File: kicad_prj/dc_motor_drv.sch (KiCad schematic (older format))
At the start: 20 parts

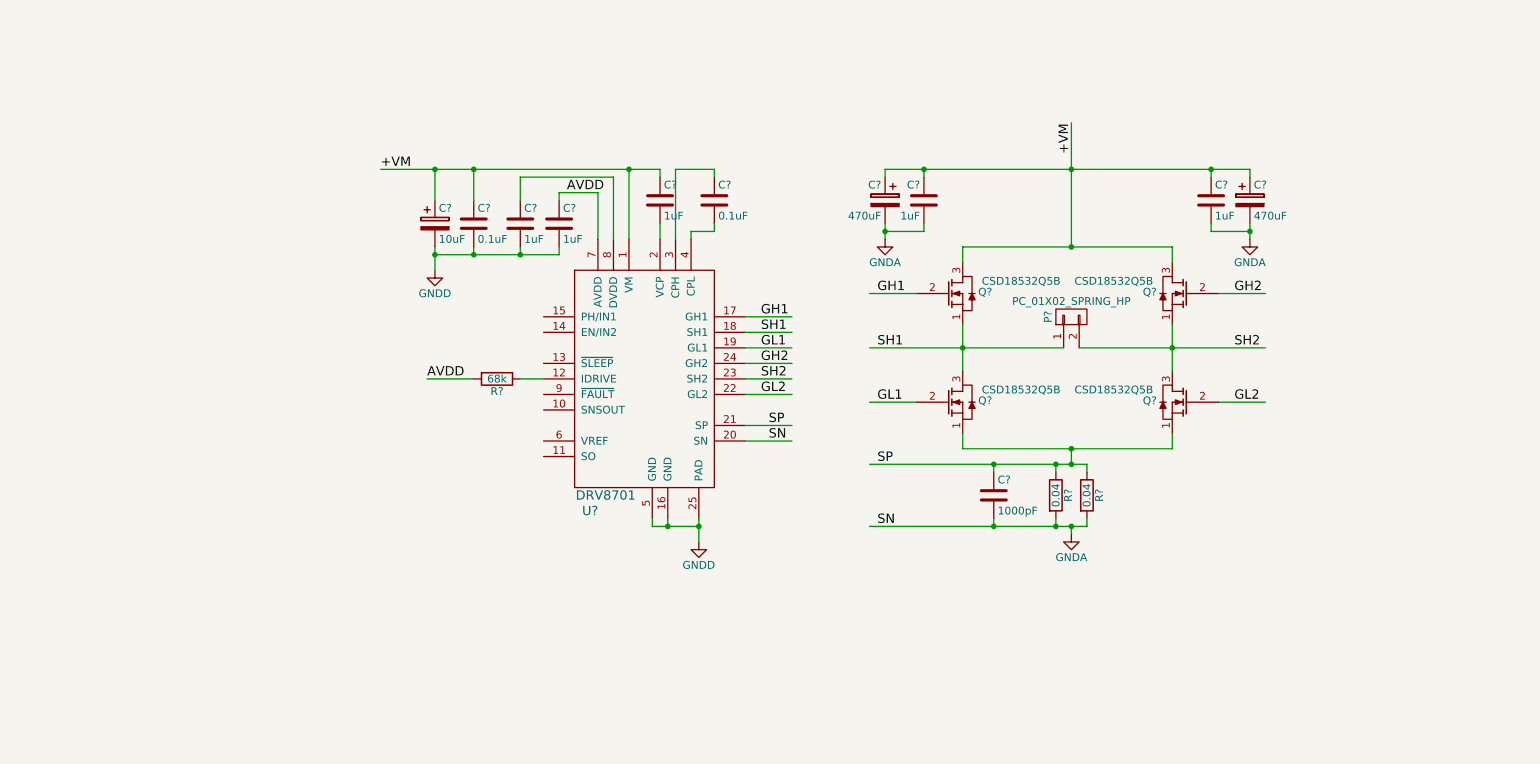
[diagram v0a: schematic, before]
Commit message: Schematics 3
Added spindle driver and sensors/limit switches.
Need to add terminals for ADC channels.
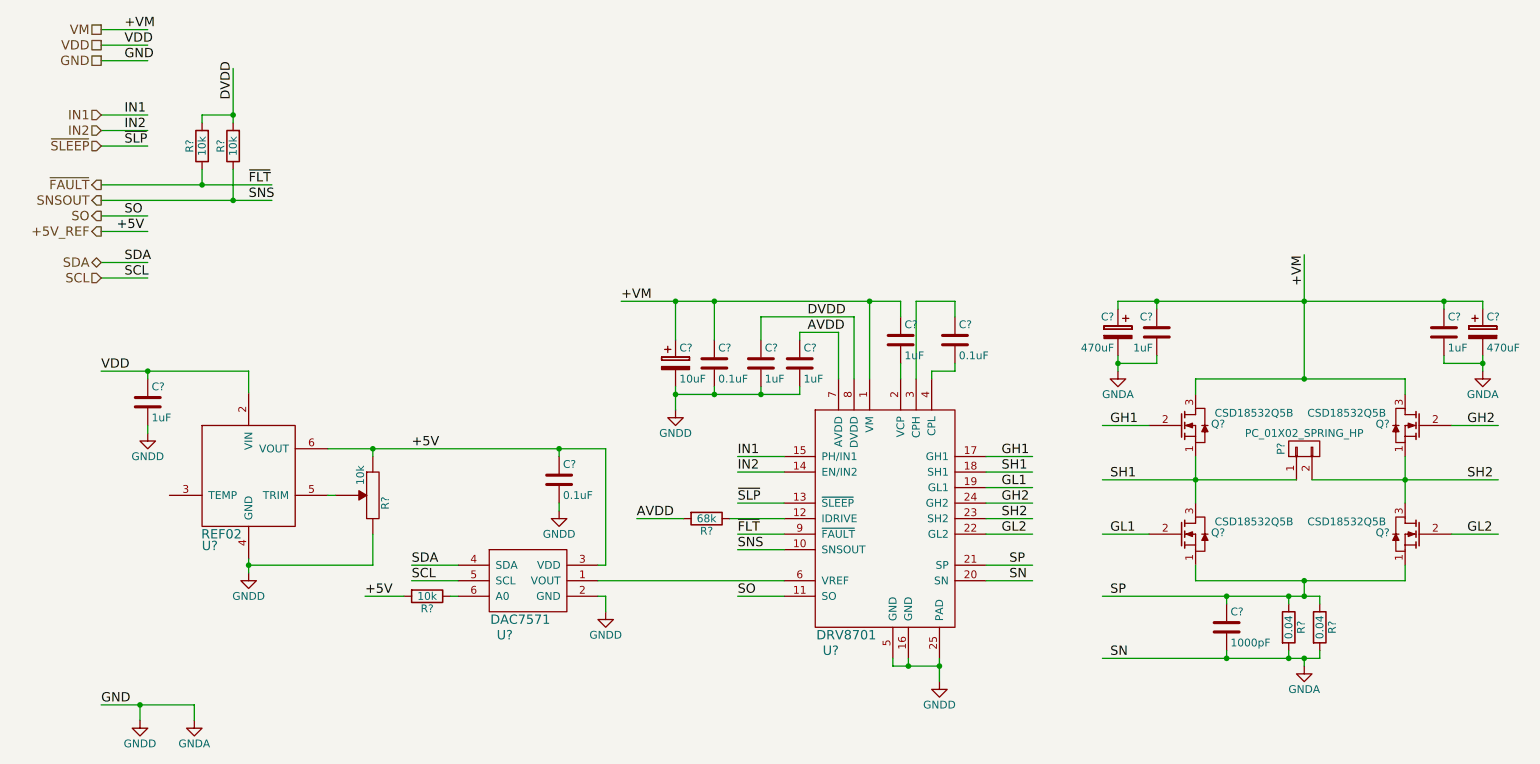
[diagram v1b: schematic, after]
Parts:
- added C?: 1uF, symbol C
- added C?: 0.1uF, symbol C
- added R?: 10k, symbol RTRM
- added R? (x3): 10k, symbol R
- added U?: DAC7571, symbol DAC7571
- added U?: REF02, symbol REF02
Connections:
- net labels added: +5V, +5V_REF, DVDD, GND, IN1, IN2, SCL, SDA, SNS, SNSOUT, SO, VDD, VM, ~FAULT, ~FLT, ~SLEEP, ~SLP
- wire segments 99 -> 120
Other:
- moved on the sheet: C?, P?, Q?, R?, U?

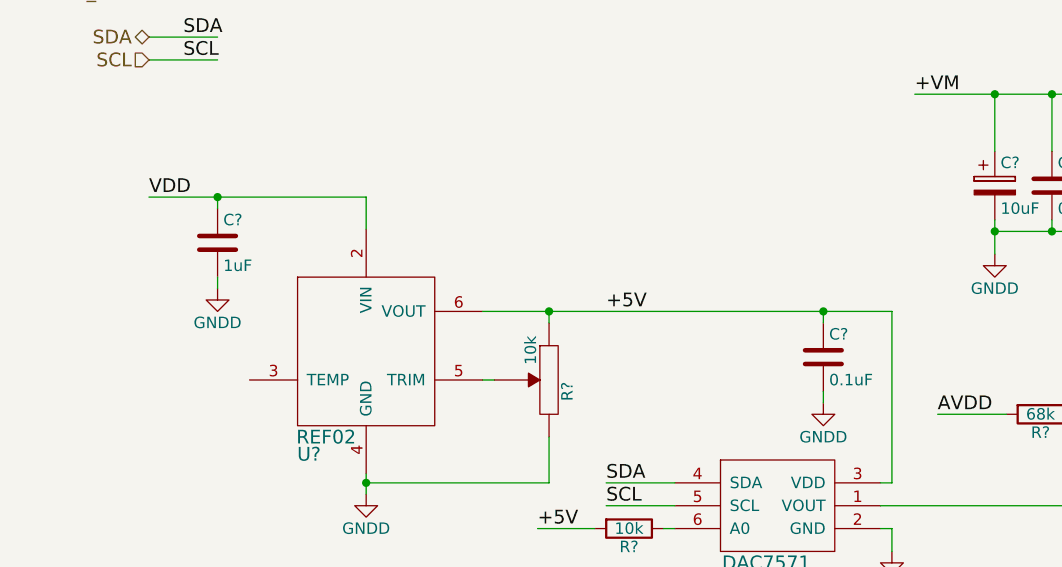
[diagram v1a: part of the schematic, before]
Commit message: Schematics 4
Finished sensor inputs.
Added DAC for stepper motor drivers.
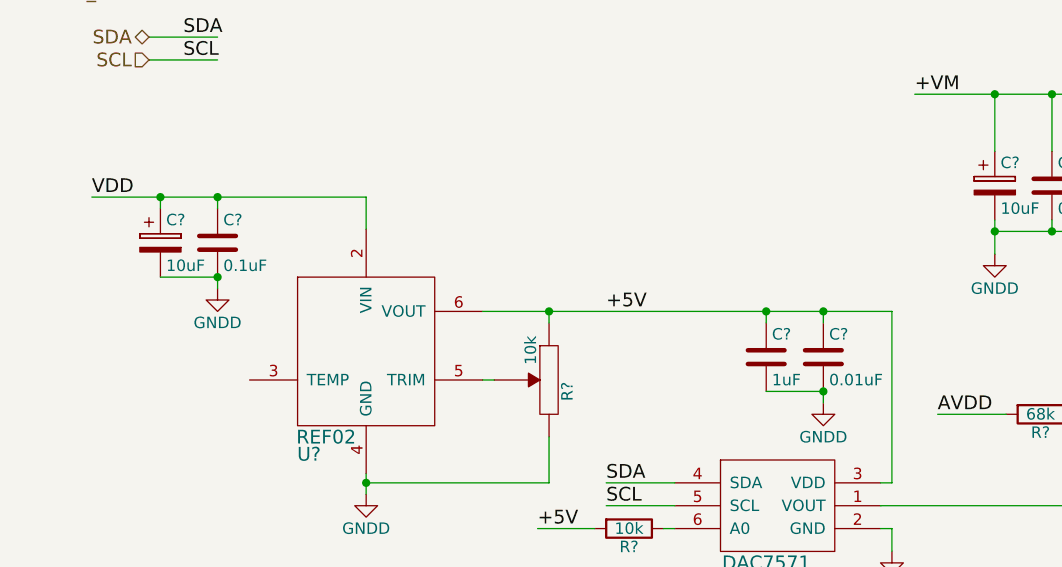
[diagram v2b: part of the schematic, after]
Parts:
- added C?: 1uF, symbol C
- added C?: 10uF, symbol CP
- C?: value 1uF -> 0.1uF
- C?: value 0.1uF -> 0.01uF
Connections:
- wire segments 120 -> 124
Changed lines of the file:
@@
 $Descr A4 11693 8268
 encoding utf-8
-Sheet 6 7
+Sheet 6 8
 Title ""
 Date ""
@@
 P 1750 3800
 F 0 "C?" H 1775 3900 50  0000 L CNN
-F 1 "1uF" H 1775 3700 50  0000 L CNN
+F 1 "0.1uF" H 1775 3700 50  0000 L CNN
 F 2 "" H 1788 3650 30  0000 C CNN
 F 3 "" H 1750 3800 60  0000 C CNN
@@
 	2400 3600 2400 3740
 Wire Wire Line
-	1450 3600 2400 3600
+	1200 3600 2400 3600
 Wire Wire Line
 	1750 3650 1750 3600
 Connection ~ 1750 3600
-Text Label 1450 3600 0    60   ~ 0
+Text Label 1200 3600 0    60   ~ 0
 VDD
 $Comp
@@
 P 4400 4300
 F 0 "C?" H 4425 4400 50  0000 L CNN
-F 1 "0.1uF" H 4425 4200 50  0000 L CNN
+F 1 "0.01uF" H 4425 4200 50  0000 L CNN
 F 2 "" H 4438 4150 30  0000 C CNN
 F 3 "" H 4400 4300 60  0000 C CNN
@@
 Wire Wire Line
 	4400 4500 4400 4450
+$Comp
+L C C?
+U 1 1 565613C4
+P 4150 4300
+F 0 "C?" H 4175 4400 50  0000 L CNN
+F 1 "1uF" H 4175 4200 50  0000 L CNN
+F 2 "" H 4188 4150 30  0000 C CNN
+F 3 "" H 4150 4300 60  0000 C CNN
+	1    4150 4300
+	1    0    0    -1
+$EndComp
+Wire Wire Line
+	4150 4150 4150 4100
+Connection ~ 4150 4100
+Wire Wire Line
+	4400 4450 4150 4450
+Connection ~ 4400 4450
+$Comp
+L CP C?
+U 1 1 565FCB4C
+P 1500 3800
+F 0 "C?" H 1525 3900 50  0000 L CNN
+F 1 "10uF" H 1525 3700 50  0000 L CNN
+F 2 "" H 1538 3650 30  0000 C CNN
+F 3 "" H 1500 3800 60  0000 C CNN
+	1    1500 3800
+	1    0    0    -1
+$EndComp
+Wire Wire Line
+	1500 3650 1500 3600
+Connection ~ 1500 3600
+Wire Wire Line
+	1500 3950 1750 3950
+Connection ~ 1750 3950
 $EndSCHEMATC

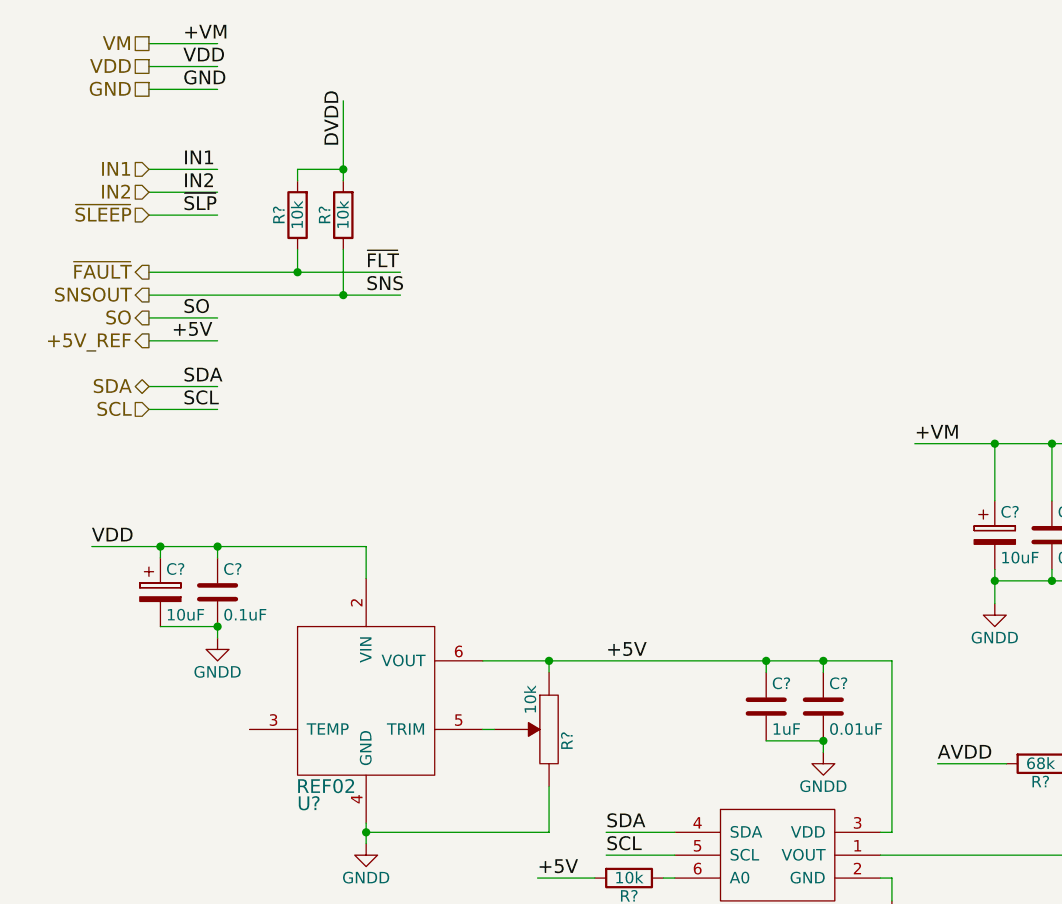
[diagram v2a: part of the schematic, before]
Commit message: Schematics 5
Started isolation part.
Selected ICs for SPI isolation and general digital I/Os.
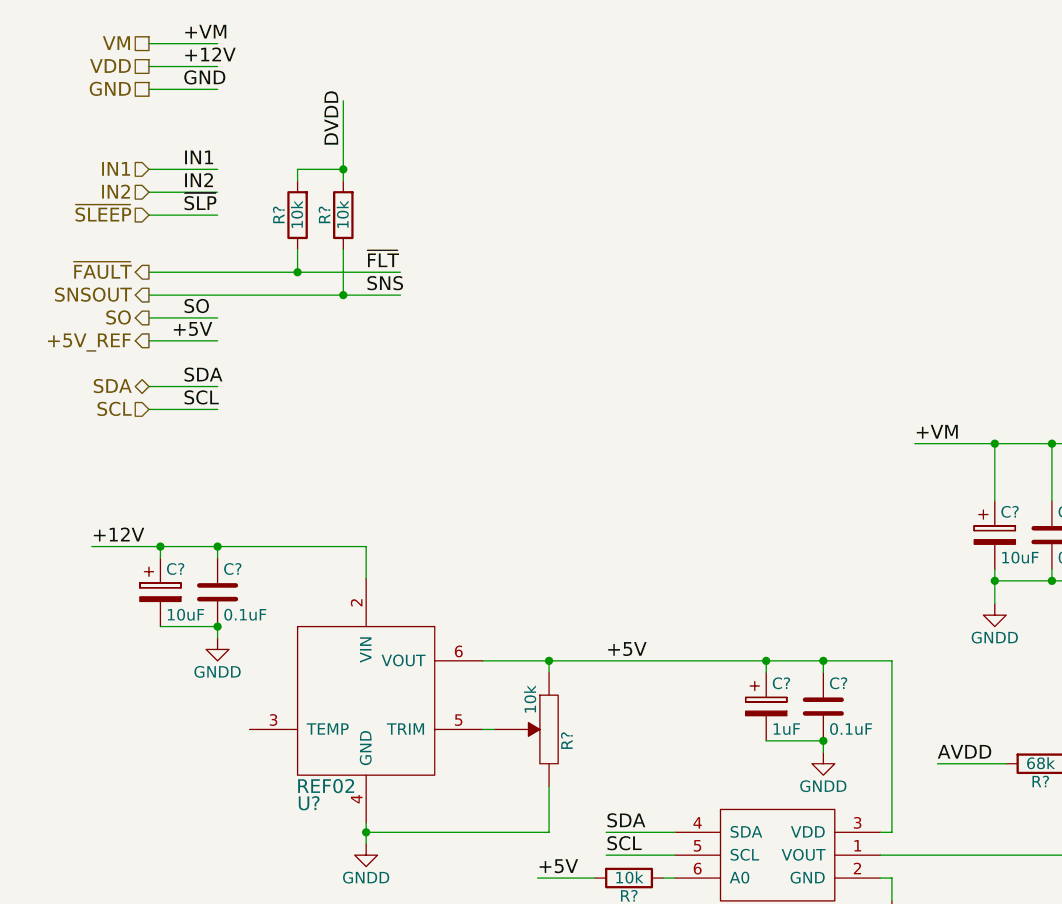
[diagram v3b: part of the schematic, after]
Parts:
- removed C?: 1uF, symbol C
- removed C?: 0.01uF, symbol C
- added C?: 1uF, symbol CP
- added C?: 0.1uF, symbol C
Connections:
- net labels added: +12V
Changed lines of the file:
@@
 $Descr A4 11693 8268
 encoding utf-8
-Sheet 6 8
+Sheet 6 9
 Title ""
 Date ""
@@
 Connection ~ 1750 3600
 Text Label 1200 3600 0    60   ~ 0
-VDD
++12V
 $Comp
 L GNDD #PWR?
@@
 +VM
 Text Label 1600 1500 0    60   ~ 0
-VDD
++12V
 Text Label 1600 1600 0    60   ~ 0
 GND
@@
 +5V
 $Comp
-L C C?
-U 1 1 565A10C6
-P 4400 4300
-F 0 "C?" H 4425 4400 50  0000 L CNN
-F 1 "0.01uF" H 4425 4200 50  0000 L CNN
-F 2 "" H 4438 4150 30  0000 C CNN
-F 3 "" H 4400 4300 60  0000 C CNN
-	1    4400 4300
-	1    0    0    -1
-$EndComp
-$Comp
 L GNDD #PWR?
 U 1 1 565A13C9
@@
 Wire Wire Line
 	4400 4500 4400 4450
-$Comp
-L C C?
-U 1 1 565613C4
-P 4150 4300
-F 0 "C?" H 4175 4400 50  0000 L CNN
-F 1 "1uF" H 4175 4200 50  0000 L CNN
-F 2 "" H 4188 4150 30  0000 C CNN
-F 3 "" H 4150 4300 60  0000 C CNN
-	1    4150 4300
-	1    0    0    -1
-$EndComp
 Wire Wire Line
 	4150 4150 4150 4100
 Connection ~ 4150 4100
-Wire Wire Line
-	4400 4450 4150 4450
-Connection ~ 4400 4450
 $Comp
 L CP C?
@@
 	1500 3950 1750 3950
 Connection ~ 1750 3950
+$Comp
+L CP C?
+U 1 1 565B9620
+P 4150 4300
+F 0 "C?" H 4175 4400 50  0000 L CNN
+F 1 "1uF" H 4175 4200 50  0000 L CNN
+F 2 "" H 4188 4150 30  0000 C CNN
+F 3 "" H 4150 4300 60  0000 C CNN
+	1    4150 4300
+	1    0    0    -1
+$EndComp
+$Comp
+L C C?
+U 1 1 565B96BD
+P 4400 4300
+F 0 "C?" H 4425 4400 50  0000 L CNN
+F 1 "0.1uF" H 4425 4200 50  0000 L CNN
+F 2 "" H 4438 4150 30  0000 C CNN
+F 3 "" H 4400 4300 60  0000 C CNN
+	1    4400 4300
+	1    0    0    -1
+$EndComp
+Wire Wire Line
+	4400 4450 4150 4450
+Connection ~ 4400 4450
 $EndSCHEMATC

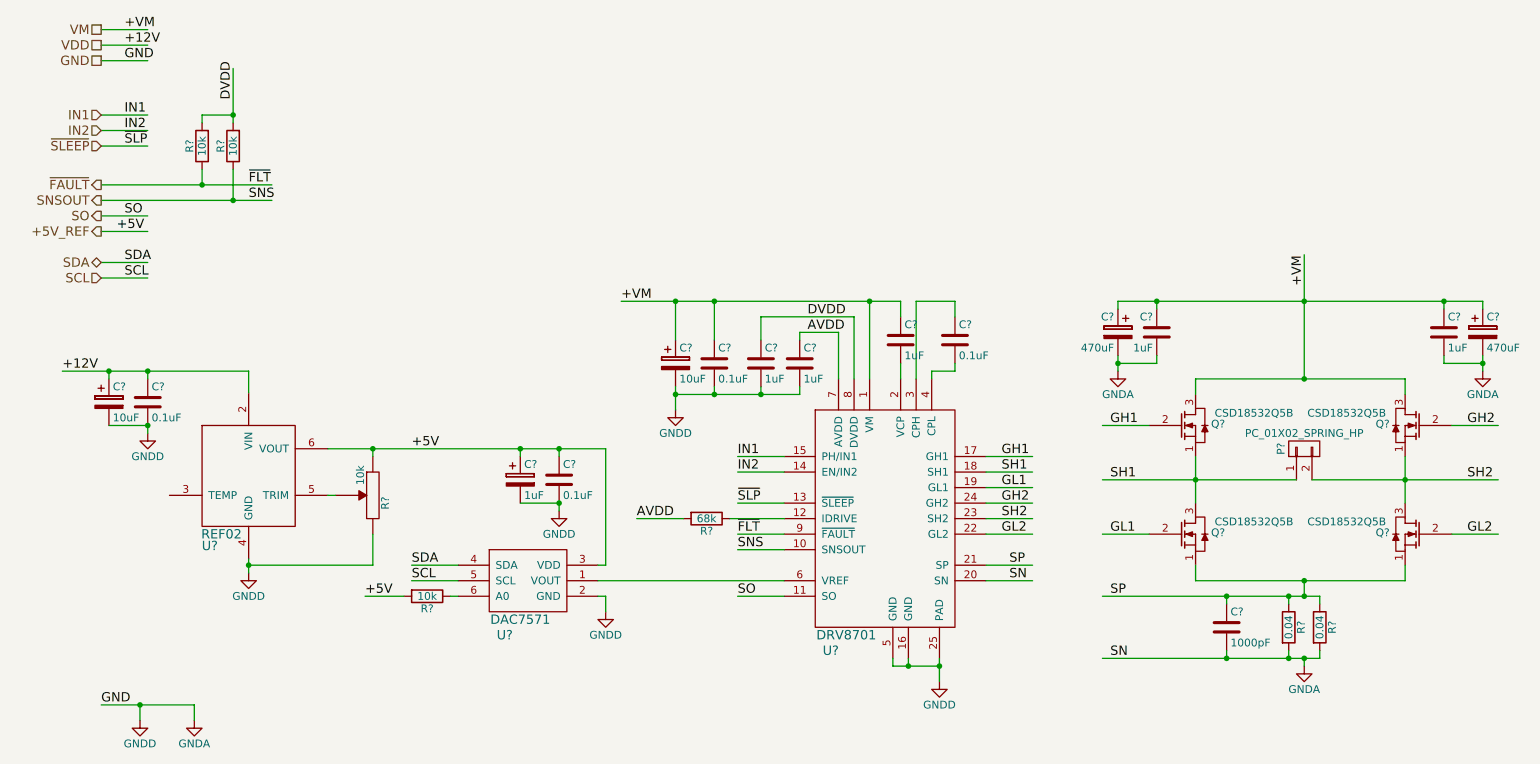
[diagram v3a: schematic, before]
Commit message: Schematics 6
Added isolation.
Misc. i2c, I/Os, spi. Need to finish iso2 sheet.
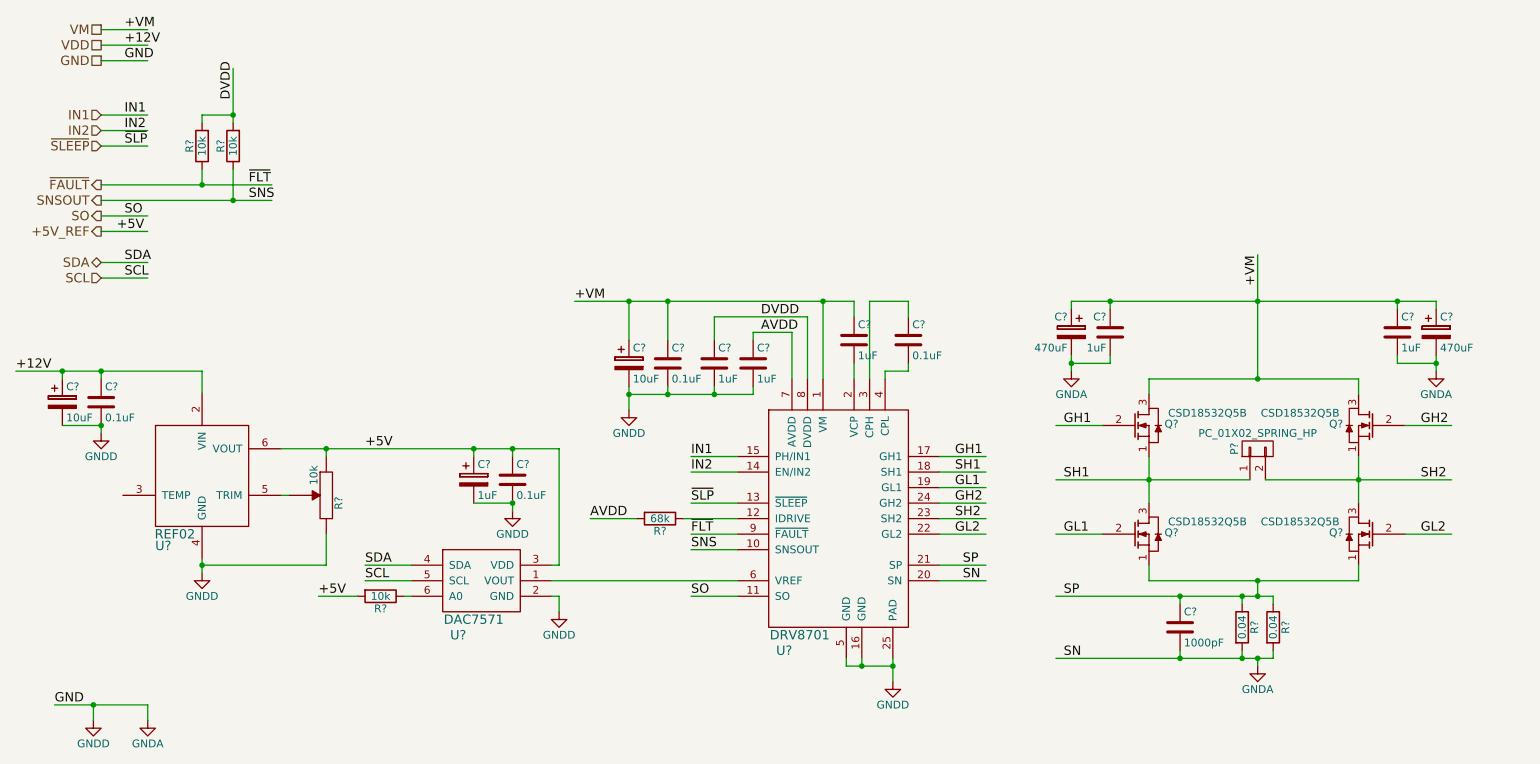
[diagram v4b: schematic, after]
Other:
- moved on the sheet: C?, P?, Q?, R?, U?
